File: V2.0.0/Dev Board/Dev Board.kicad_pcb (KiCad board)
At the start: 2 copper layers, 50 x 80 mm, 62 parts, among them J1 PICKIT4 Conn, J2 I2C Conn, J3 UART Conn, J4 SPI Conn, J5 CAN Conn, J6 PORT B, J7 Analog, U1 MCP2551-I-SN, U2 PIC18F25K80_ISS, U3 NCP1117-5.0_TO252, Y1 20MHz

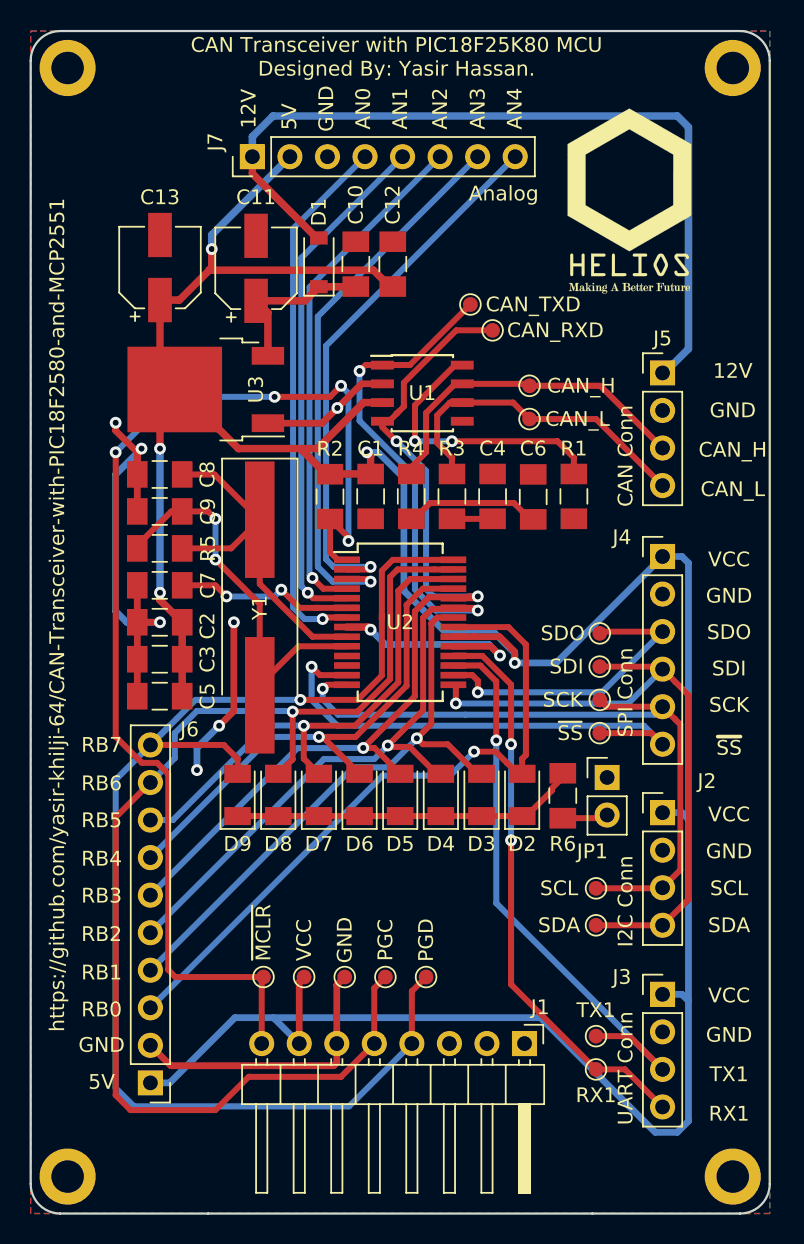
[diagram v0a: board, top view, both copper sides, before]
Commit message: PGD and PGC Glitch Removed
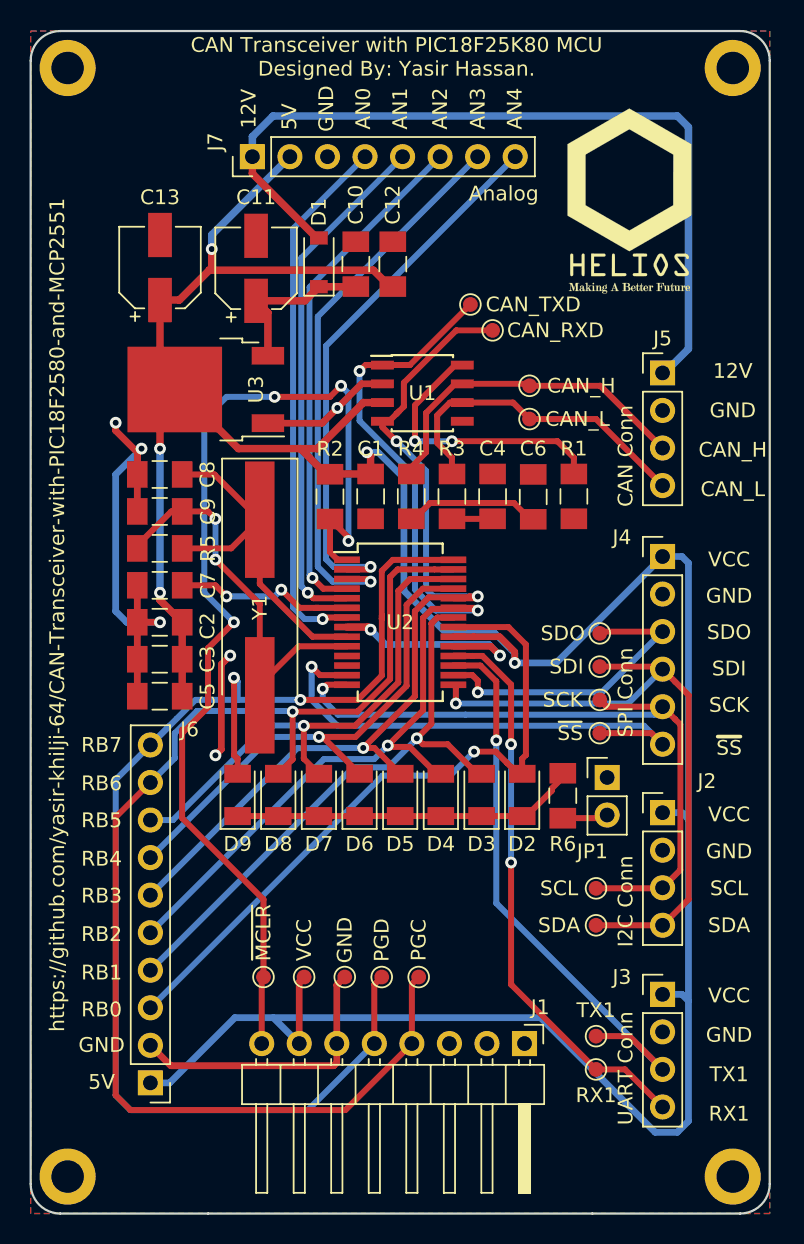
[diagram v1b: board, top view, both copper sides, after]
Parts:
- moved TP2 3.00 mm to (113.8, 124.0)
- moved TP3 2.25 mm to (116.2, 124.0)
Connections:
- J1 pad 4: /RB7_PGD -> /RB6_PGC
- J1 pad 5: /RB6_PGC -> /RB7_PGD
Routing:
- net /~MCLR: track 81.7 -> 73.6 mm
- net GND: track 86.3 -> 82.4 mm, vias 9 -> 8
- net /RB6_PGC: track 82.9 -> 85.3 mm
- net /RB7_PGD: track 90.6 -> 89.3 mm, vias 1 -> 2
